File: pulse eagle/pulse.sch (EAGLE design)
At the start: 22 parts, among them J1 ISP Touch, U1 ATMEGA328P, Y1 8MHz

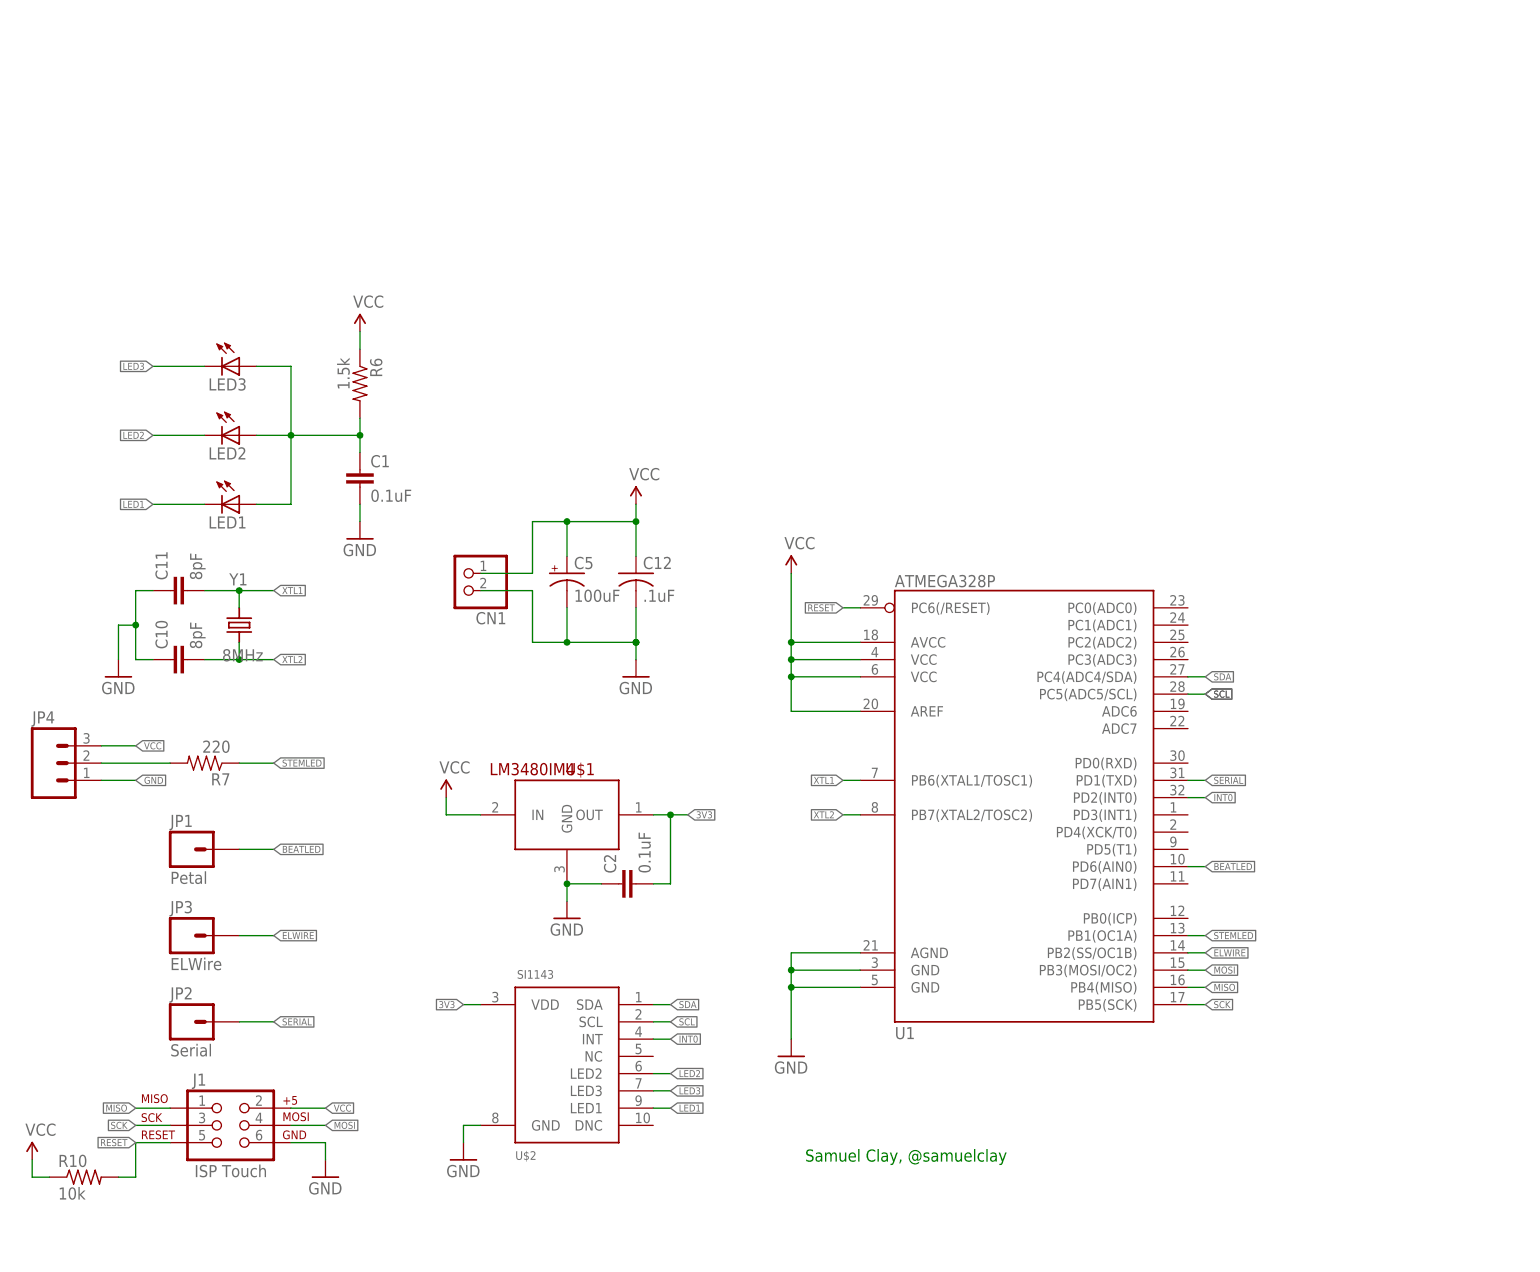
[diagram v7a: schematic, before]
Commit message: Revision 4 of the board now connects all 5v, 12v, and 3.3v devices. Revision 1 of the sensor board.
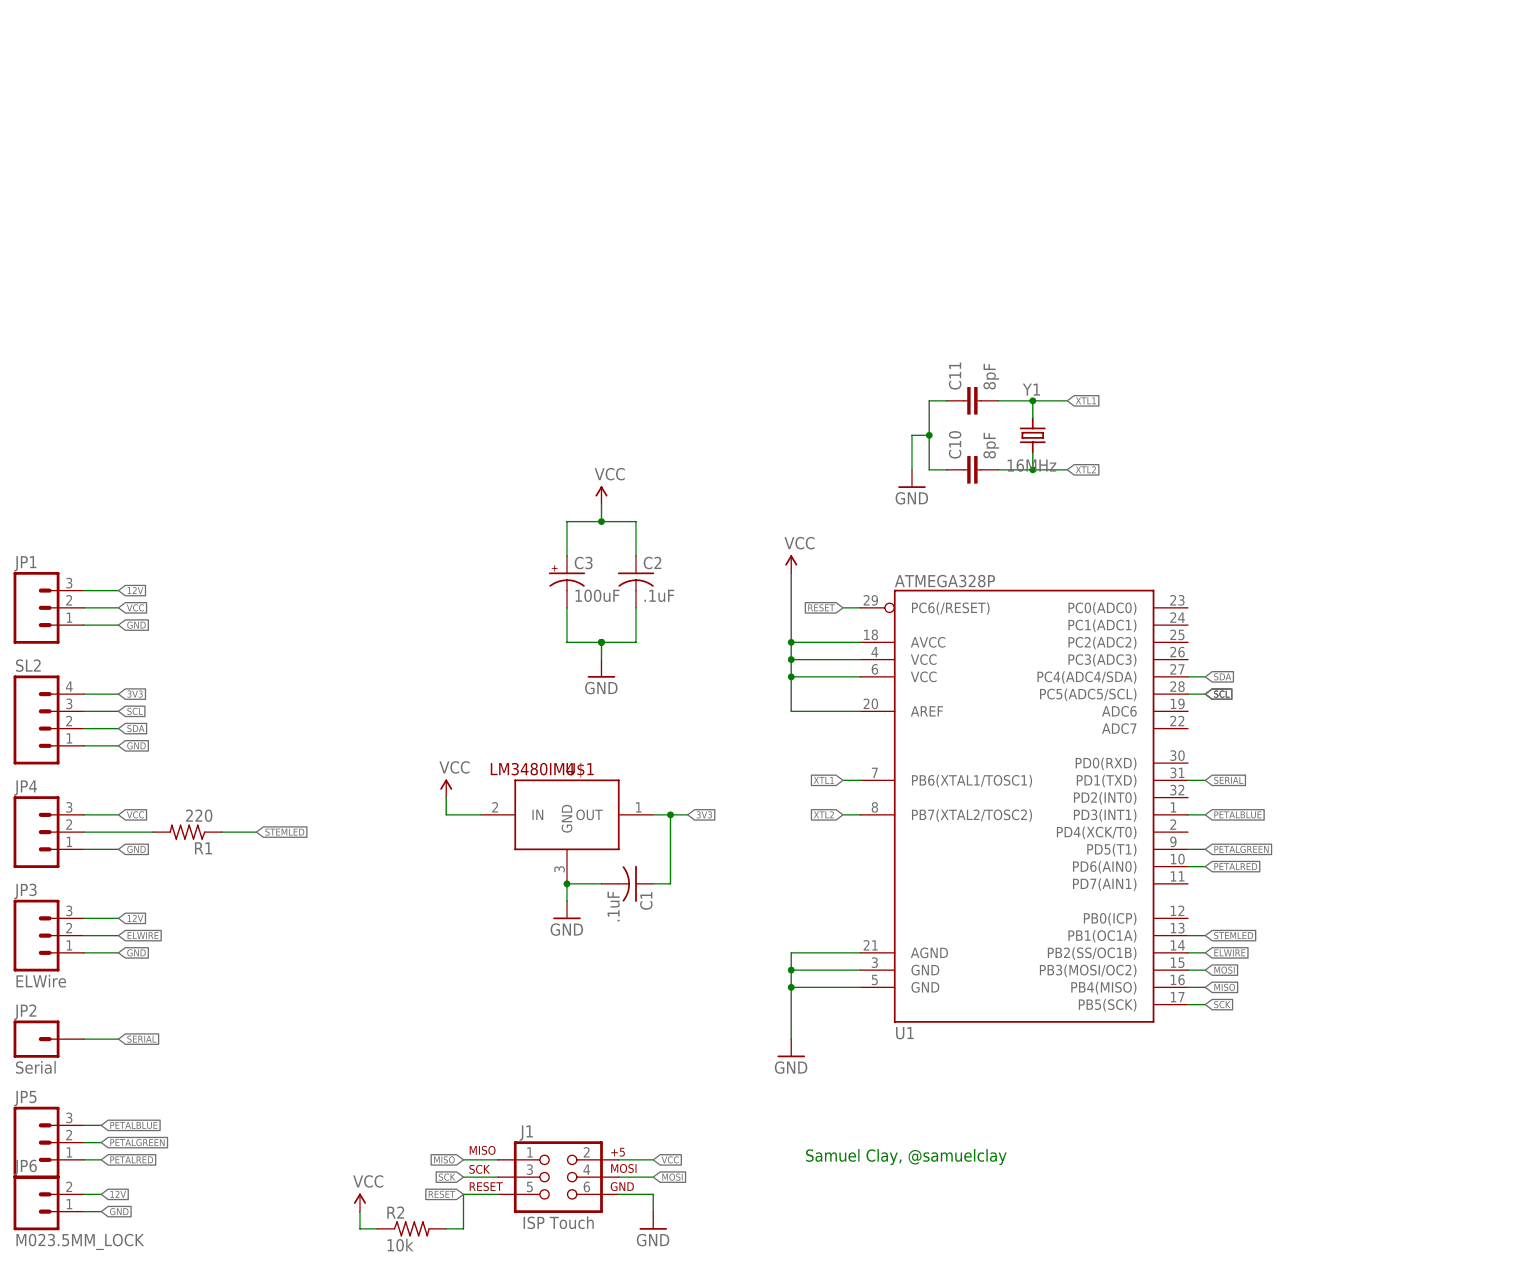
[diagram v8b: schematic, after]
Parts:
- removed C12: .1uF, adafruit:C-USC0805
- removed CN1: (no value), adafruit:JST_2PIN-THM
- removed LED1, LED2, LED3: (no value), SparkFun-LED:LED1206
- removed R10: 10k, adafruit:R-US_R0805
- removed R6: 1.5k, SparkFun-Resistors:220-5%
- removed R7: 220, SparkFun-Resistors:220-5%
- removed U$2: SI1143, pulse:SI1143
- added JP5: (no value), SparkFun-Connectors:M03POLAR_LOCK
- added JP6: M023.5MM_LOCK, SparkFun-Connectors:M023.5MM_LOCK
- added R1: 220, resistor:R-US_R0805
- added R2: 10k, adafruit:R-US_R0805
- added SL2: (no value), SparkFun-Connectors:M04POLAR_LOCK
- C1, C2: value 0.1uF -> .1uF; device SparkFun-Capacitors:.1UF-CER -> adafruit:C-USC0805
- JP1: value Petal -> (none); device SparkFun-Connectors:M01PTH -> SparkFun-Connectors:M03SCREW_LOCK
- JP3: device SparkFun-Connectors:M01PTH -> SparkFun-Connectors:M03POLAR_LOCK
- JP4: device SparkFun-Connectors:M03PTH -> SparkFun-Connectors:M03POLAR_LOCK
- Y1: value 8MHz -> 16MHz
- renumbered C5 to C3
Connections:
- removed net BEATLED: JP1.1, U1.PD6(AIN0)
- removed net INT0: U$2.INT, U1.PD2(INT0)
- removed net LED1: LED1.C, U$2.LED1
- removed net LED2: LED2.C, U$2.LED2
- removed net LED3: LED3.C, U$2.LED3
- removed net N$2: C1.1, LED1.A, LED2.A, LED3.A, R6.2
- new net 12V: JP1.3, JP3.3, JP6.2
- new net PETALBLUE: JP5.3, U1.PD3(INT1)
- new net PETALGREEN: JP5.2, U1.PD5(T1)
- new net PETALRED: JP5.1, U1.PD6(AIN0)
- net 3V3: now also C1.1, SL2.4; no longer C2.2, U$2.VDD
- net ELWIRE: now also JP3.2; no longer JP3.1
- net GND: now also C2.2, JP1.1, JP3.1, JP6.1, SL2.1; no longer C12.2, C2.1, CN1.1, U$2.GND
- net N$7: now also R1.2; no longer R7.2
- net RESET: now also R2.2; no longer R10.2
- net SCL: now also SL2.3; no longer U$2.SCL
- net SDA: now also SL2.2; no longer U$2.SDA
- net STEMLED: now also R1.1; no longer R7.1
- net VCC: now also C2.1, JP1.2, R2.1; no longer C12.1, CN1.2, R10.1, R6.1
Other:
- moved on the sheet: C1, C10, C11, C2, J1, JP2, JP4, Y1
